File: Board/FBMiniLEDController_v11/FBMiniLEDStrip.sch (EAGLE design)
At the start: 20 parts, among them J4 POWER_JACKPTH_LOCK, U1 74LVC2T45

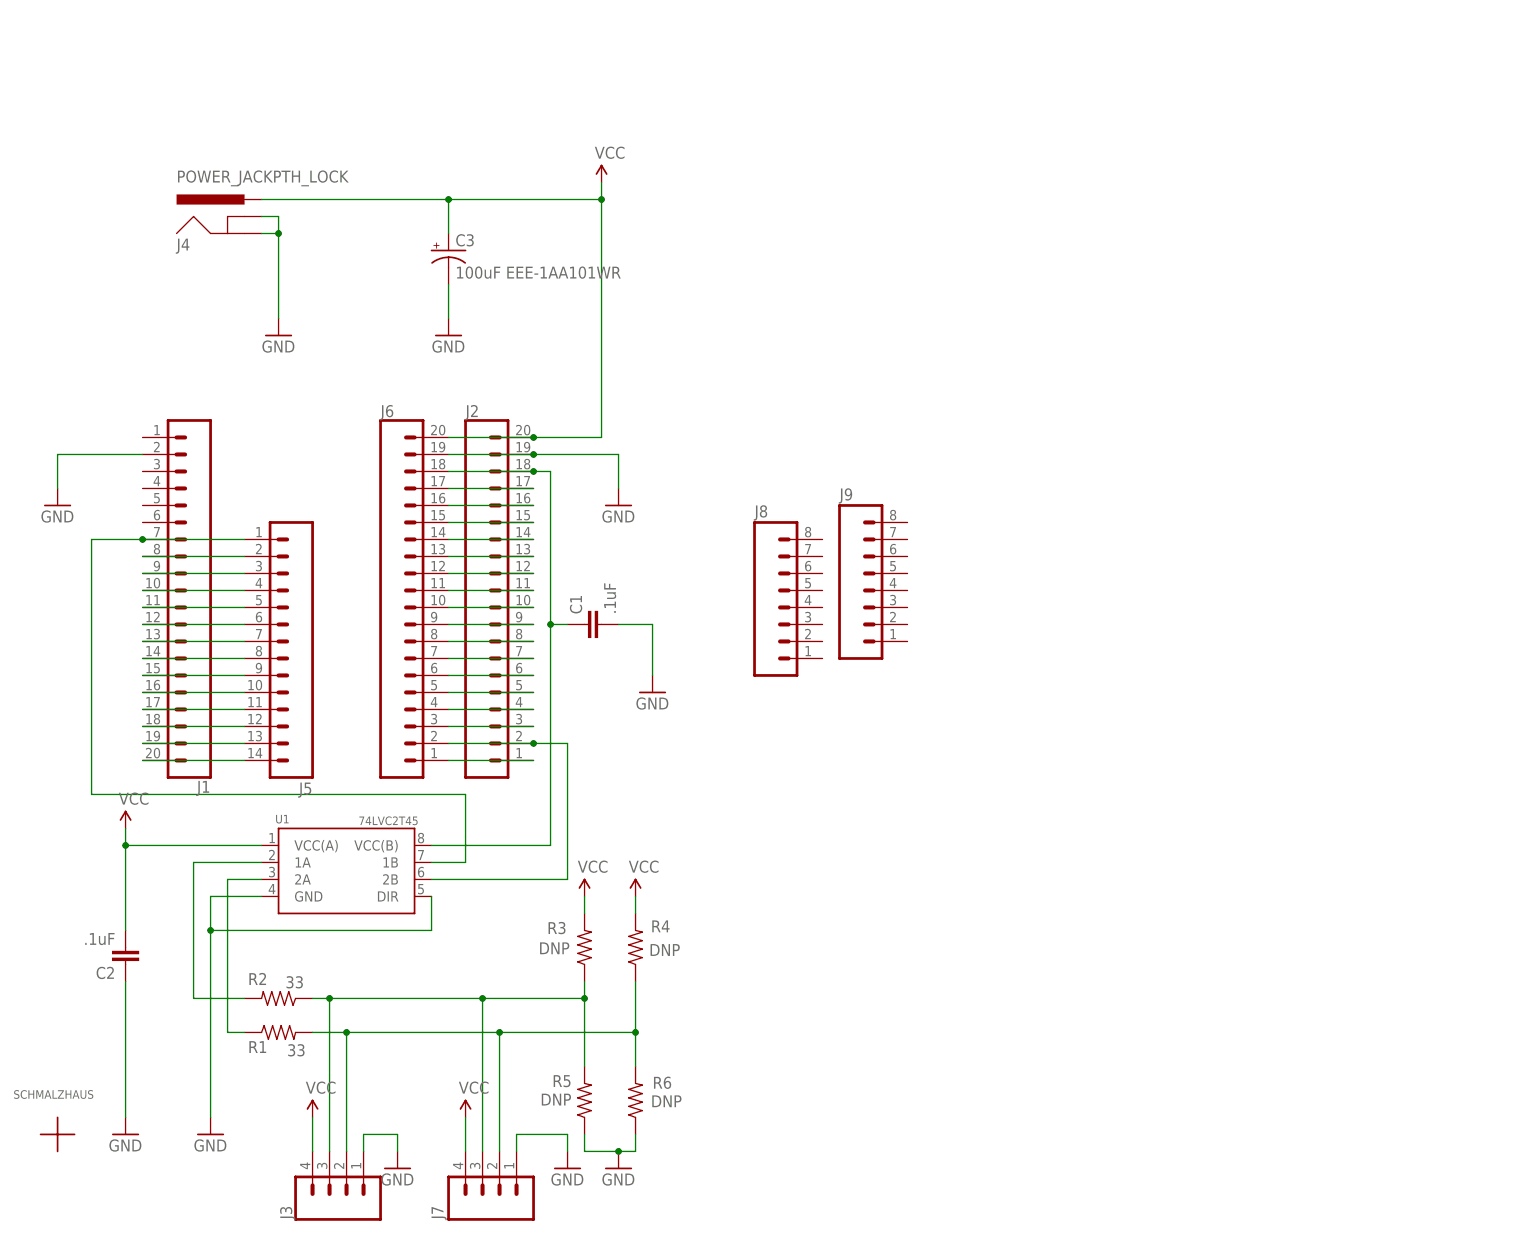
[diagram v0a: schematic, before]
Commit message: Updated v1.1 schematic with a lot more good information - no board changes.
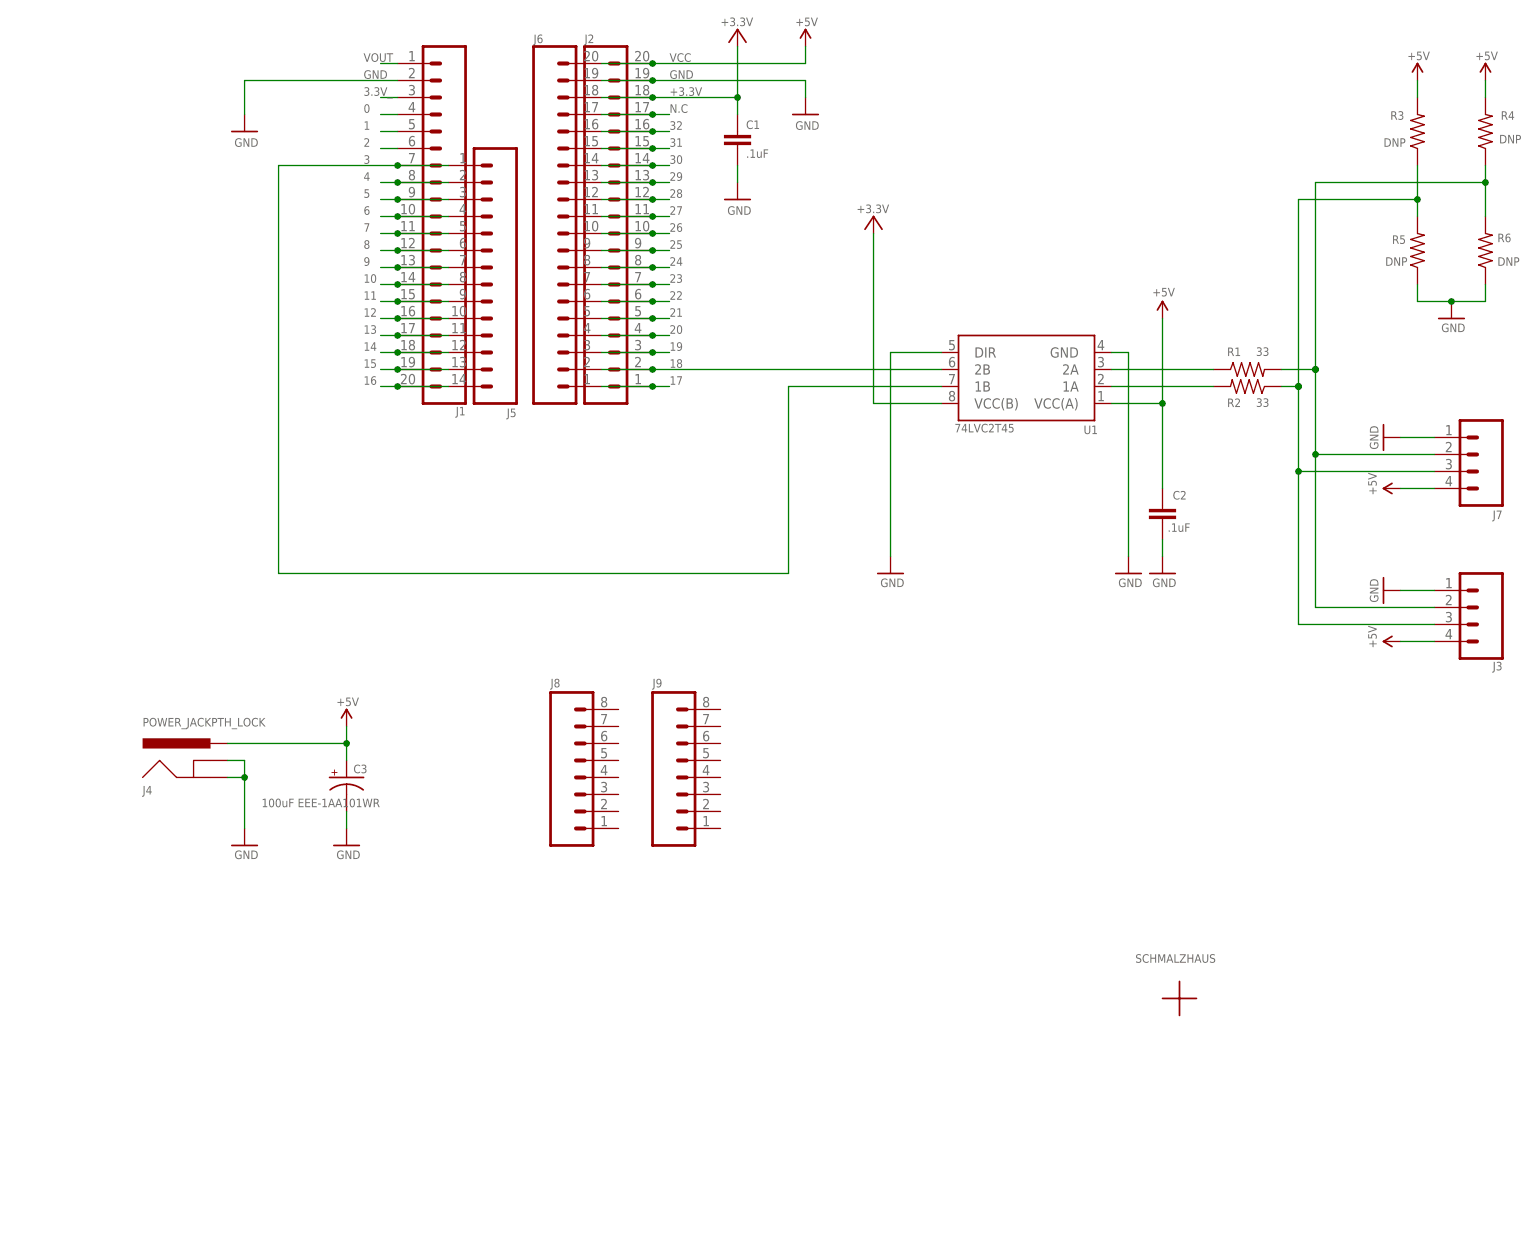
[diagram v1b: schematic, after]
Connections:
- net N$10 renamed 4
- net N$11 renamed 5
- net N$12 renamed 6
- net N$13 renamed 7
- net N$14 renamed 8
- net N$15 renamed 9
- net N$16 renamed 10
- net N$17 renamed 11
- net N$18 renamed 12
- net N$19 renamed 13
- net N$20 renamed 14
- net N$21 renamed 15
- net N$22 renamed 16
- net N$26 renamed N.C
- net N$27 renamed 32
- net N$28 renamed 31
- net N$29 renamed 30
- net N$30 renamed 29
- net N$31 renamed 28
- net N$32 renamed 27
- net N$33 renamed 26
- net N$34 renamed 25
- net N$35 renamed 24
- net N$36 renamed 23
- net N$37 renamed 22
- net N$38 renamed 21
- net N$39 renamed 20
- net N$40 renamed 19
- net N$41 renamed 18
- net N$42 renamed 17
- net N$9 renamed 3
- removed net N$25: C1.1, J2.18, J6.18, U1.VCC(B)
- new net +3.3V: C1.1, J2.18, J6.18
- new net +3V3: U1.VCC(B)
- new net 0: J1.4
- new net 1: J1.5
- new net 2: J1.6
- new net 3.3V_: J1.3
- new net VOUT: J1.1
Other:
- note added: "+5V"
- note added: ".1" header"
- note added: "3.5mm Screw Terminals"
- note added: "5V Power Input"
- note added: "Both DotStar and NeoPixels can be used with this board. NeoPixel: Use +5V, GND, and DAT pins on connector. In code, use output pin 18. DotStar: Use +5V, GND, DAT and CLK pins In code, use defualt SPI port"
- note added: "CLK"
- note added: "Change List v1.0 6/16/2017 Inital release v1.1 6/24/2017 - Removed on/off switch - Centered barrel jack under FBMini - Flipped FBMini around so USB is on power end - Added series resistors in CLK and DAT - Added bus biasing resistors - Added 100uF 5V bulk cap"
- note added: "DAT"
- note added: "Designed by Brian Schmalz of Schmalz Haus LLC brian@schmalzhaus.com For Guy McCarthy of Microchip"
- note added: "Extra Prototyping Holes"
- note added: "FBMini LED Controller Board v1.1"
- note added: "Fubarino Mini"
- note added: "Fubarino Mini can be purchased here : http://www.microchipdirect.com/productsearch.aspx?Keywords=TCHIP011"
- note added: "Fubarino Mini pin table located here : https://github.com/fubarino/fubarino.github.com/blob/master/mini/docs/FubarinoMiniUserRefManual.pdf"
- note added: "Fubinaro Mini Pin Numbers"
- note added: "GND"
- note added: "LED Output Connectors"
- note added: "Level Shifter (3.3V -> 5V)"
- note added: "Optional LED Bus Biasing"
- note added: "USB Connector"
- note added: "Use extra sets of FBMini pin holes to add extra inputs our outputs for your project"
- moved on the sheet: C1, C2, C3, J1, J2, J3, J4, J5, J6, J7, J8, J9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
